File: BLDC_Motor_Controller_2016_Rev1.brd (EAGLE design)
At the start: 112.4 x 80 mm, 103 parts, among them J1 SERVOMOLEX_SL_THRU_HOLE, J3 APP_2POS_CONFIG5V_HORIZ, Q1 MOSFET-NCHANNELFQP30N06L, Q2 MOSFET-NCHANNELFQP30N06L, Q3 MOSFET-NCHANNELFQP30N06L, Q4 MOSFET-NCHANNELFQP30N06L, Q5 MOSFET-NCHANNELFQP30N06L, Q6 MOSFET-NCHANNELFQP30N06L, Q7 MOSFET-PCHANNEL, Q8 MOSFET-PCHANNEL

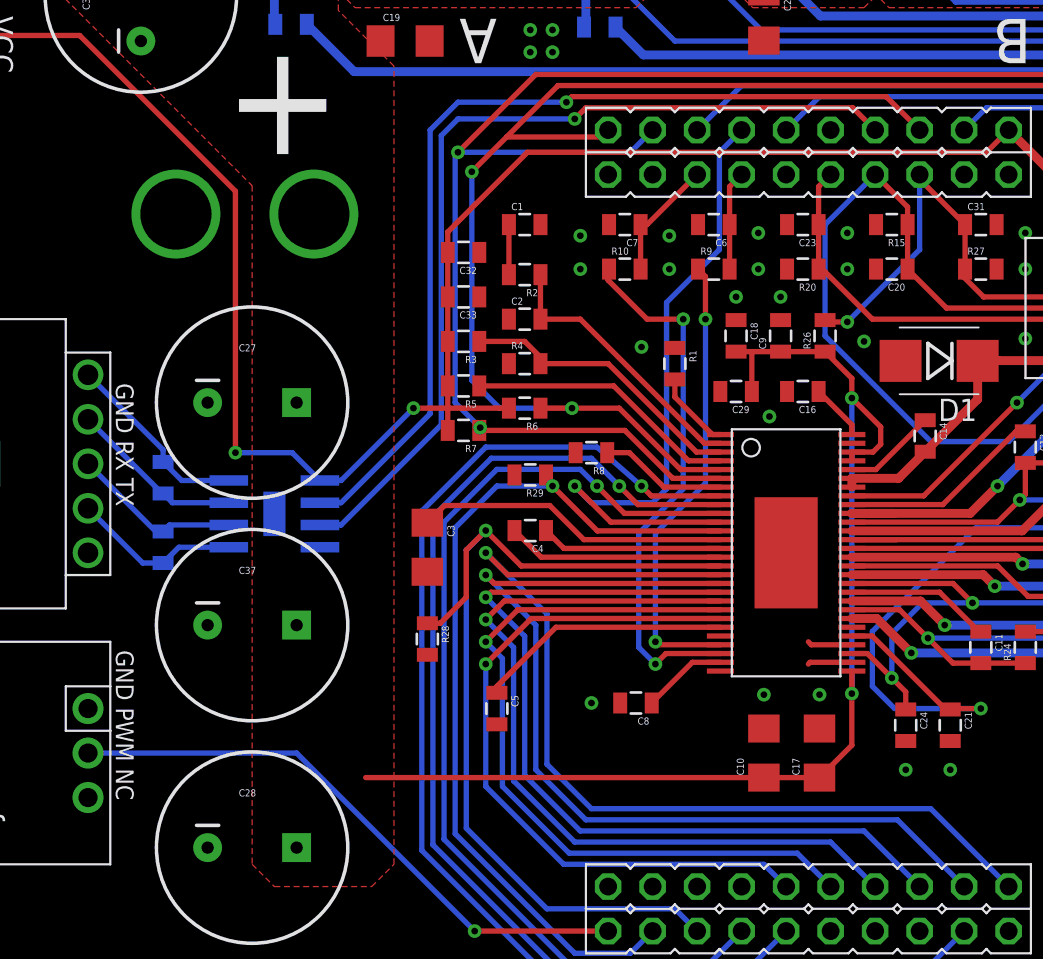
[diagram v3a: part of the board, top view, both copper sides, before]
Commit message: Minor routing changes
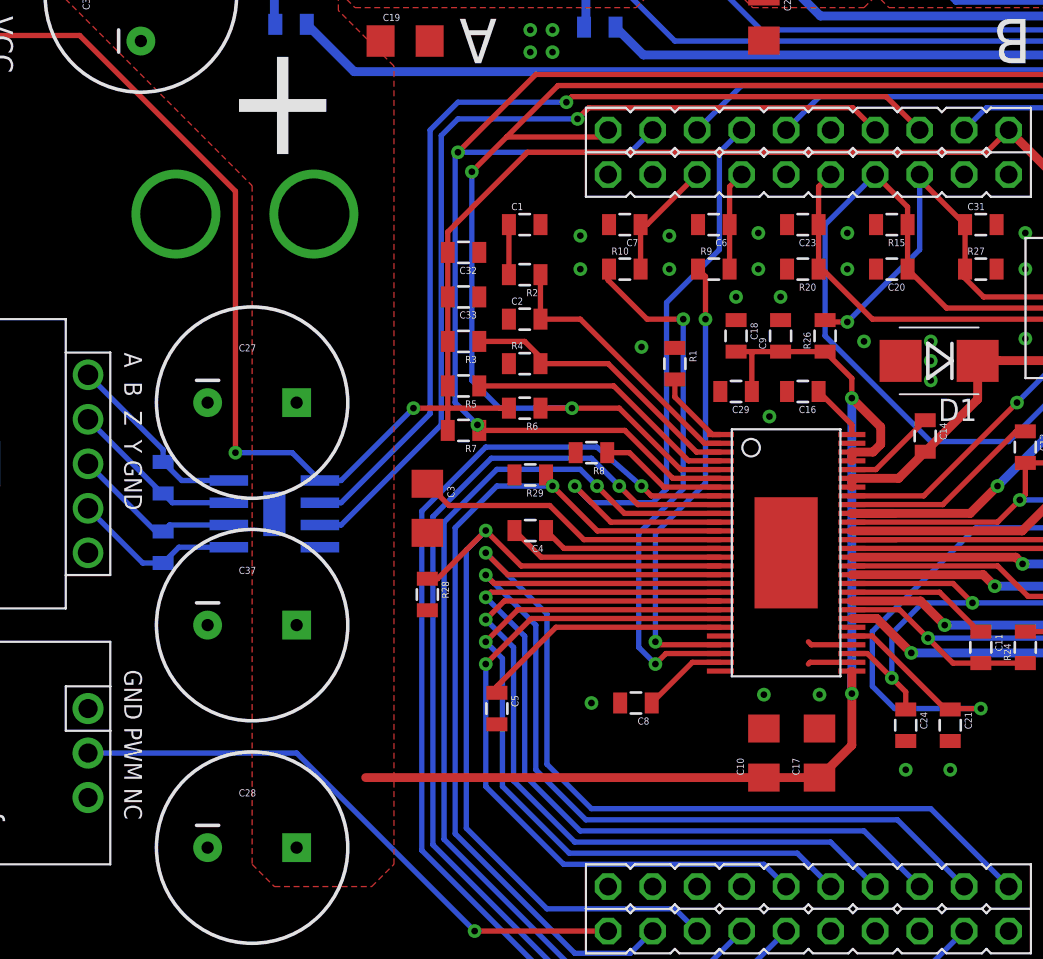
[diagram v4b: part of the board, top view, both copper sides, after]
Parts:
- moved R28 2.54 mm to (30.3, 23.0)
- moved C3 2.22 mm to (30.3, 27.9)
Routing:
- net EN_GATE: track 54.4 -> 51.8 mm
- net GND: vias 32 -> 35
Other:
- board text added: "A B Z Y GND"
- board text removed: "GND RX TX"
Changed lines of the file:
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@@
 <text x="5.3975" y="56.03875" size="1.27" layer="21" font="vector" rot="SR270">VCC</text>
 <text x="95.09125" y="19.3675" size="0.8128" layer="21" font="vector" rot="R90">Vcc C   B   A GND</text>
-<text x="12.54125" y="19.84375" size="1.016" layer="21" font="vector" rot="SR270">GND PWM NC</text>
+<text x="13.0175" y="18.7325" size="1.016" layer="21" font="vector" rot="SR270">GND PWM NC</text>
 <text x="101.9175" y="47.625" size="1.27" layer="21" font="vector" rot="SR90">FAULT</text>
 <text x="101.9175" y="41.5925" size="1.27" layer="21" font="vector" rot="SR90">OCTW</text>
@@
 <dimension x1="110.16" y1="-1.27" x2="110.16" y2="78.73" x3="127" y3="38.73" textsize="1.778" layer="47" unit="inch"/>
 <dimension x1="-3.4925" y1="-1.27" x2="110.16" y2="-1.27" x3="53.33375" y3="-21.59" textsize="1.778" layer="47" unit="inch"/>
-<text x="12.54125" y="35.08375" size="1.016" layer="21" font="vector" rot="SR270">GND RX TX</text>
 <text x="77.47" y="5.08" size="1.27" layer="21" font="vector" align="bottom-center">Missouri S&amp;T
 Mars Rover Design Team
@@
 Cameron Nichols
 </text>
+<text x="13.0175" y="36.83" size="1.016" layer="21" font="vector" rot="SR270">A  B  Z  Y GND</text>
 </plain>
 <attributes>
@@
 <element name="C26" library="SparkFun-Passives" package="0805" value="0.1u" x="66.9925" y="20.0025" rot="R270"/>
 <element name="C29" library="SparkFun-Passives" package="0805" value="0.1u" x="47.9425" y="34.6075" rot="R180"/>
-<element name="C3" library="SparkFun-Passives" package="1206" value="2.2u" x="30.32125" y="25.7175" rot="R270"/>
+<element name="C3" library="SparkFun-Passives" package="1206" value="2.2u" x="30.32125" y="27.94" rot="R270"/>
 <element name="C30" library="SparkFun-Passives" package="0805" value="0.01u" x="2.06375" y="65.88125" rot="R180"/>
 <element name="C31" library="SparkFun-Passives" package="0805" value="0.1u" x="61.9125" y="44.1325"/>
@@
 <element name="R26" library="SparkFun-Passives" package="0805" value="34.8k" x="53.0225" y="37.7825" rot="R90"/>
 <element name="R27" library="SparkFun-Passives" package="0805" value="4.99k" x="61.9125" y="41.5925"/>
-<element name="R28" library="SparkFun-Passives" package="0805" value="1k" x="30.32125" y="20.47875" rot="R270"/>
+<element name="R28" library="SparkFun-Passives" package="0805" value="1k" x="30.32125" y="23.01875" rot="R270"/>
 <element name="R29" library="SparkFun-Passives" package="0805" value="1k" x="36.195" y="29.845" rot="R180"/>
 <element name="R3" library="SparkFun-Passives" package="0805" value="31.6k" x="32.385" y="37.465" rot="R180"/>
@@
 <via x="44.1325" y="41.5925" extent="1-16" drill="0.381" shape="square"/>
 <via x="49.8475" y="33.17875" extent="1-16" drill="0.381" shape="square"/>
+<via x="59.055" y="37.465" extent="1-16" drill="0.381" shape="square"/>
+<via x="59.055" y="36.35375" extent="1-16" drill="0.381" shape="square"/>
+<via x="59.055" y="35.2425" extent="1-16" drill="0.381" shape="square"/>
 </signal>
 <signal name="N$3">
@@
 <wire x1="41.91" y1="48.26" x2="43.18" y2="49.53" width="0.3048" layer="16"/>
 <wire x1="33.285" y1="32.385" x2="33.285" y2="32.49125" width="0.3048" layer="1"/>
-<wire x1="33.285" y1="32.49125" x2="33.3375" y2="32.54375" width="0.3048" layer="1"/>
-<via x="33.3375" y="32.54375" extent="1-16" drill="0.381"/>
-<wire x1="33.3375" y1="32.54375" x2="31.90875" y2="33.9725" width="0.3048" layer="16"/>
+<wire x1="33.285" y1="32.49125" x2="33.17875" y2="32.7025" width="0.3048" layer="1"/>
+<via x="33.17875" y="32.7025" extent="1-16" drill="0.381"/>
+<wire x1="33.17875" y1="32.7025" x2="31.90875" y2="33.9725" width="0.3048" layer="16"/>
 <wire x1="31.90875" y1="33.9725" x2="31.90875" y2="48.10125" width="0.3048" layer="16"/>
 <wire x1="31.90875" y1="48.10125" x2="32.0675" y2="48.26" width="0.3048" layer="16"/>
@@
 <wire x1="47.05" y1="26.15" x2="39.255" y2="26.15" width="0.3048" layer="1"/>
 <wire x1="39.255" y1="26.15" x2="37.30625" y2="28.09875" width="0.3048" layer="1"/>
-<wire x1="37.30625" y1="28.09875" x2="31.3025" y2="28.09875" width="0.3048" layer="1"/>
-<wire x1="31.3025" y1="28.09875" x2="30.32125" y2="27.1175" width="0.3048" layer="1"/>
+<wire x1="37.30625" y1="28.09875" x2="31.5625" y2="28.09875" width="0.3048" layer="1"/>
+<wire x1="31.5625" y1="28.09875" x2="30.32125" y2="29.34" width="0.3048" layer="1"/>
 </signal>
 <signal name="EN_GATE">
@@
 <wire x1="44.45" y1="5.08" x2="37.1475" y2="5.08" width="0.3048" layer="16"/>
 <wire x1="37.1475" y1="5.08" x2="32.54375" y2="9.68375" width="0.3048" layer="16"/>
-<wire x1="30.32125" y1="21.37875" x2="31.0625" y2="21.37875" width="0.3048" layer="1"/>
-<wire x1="31.0625" y1="21.37875" x2="32.54375" y2="22.86" width="0.3048" layer="1"/>
-<wire x1="32.54375" y1="22.86" x2="32.54375" y2="25.55875" width="0.3048" layer="1"/>
-<wire x1="32.54375" y1="25.55875" x2="33.655" y2="26.67" width="0.3048" layer="1"/>
+<wire x1="30.32125" y1="23.91875" x2="30.90375" y2="23.91875" width="0.3048" layer="1"/>
+<wire x1="30.90375" y1="23.91875" x2="33.655" y2="26.67" width="0.3048" layer="1"/>
 </signal>
 <signal name="INH_A">
@@
 <contactref element="C37" pad="1"/>
 <contactref element="D6" pad="A"/>
-<wire x1="54.55" y1="31.15" x2="54.55" y2="30.65" width="0.3048" layer="1"/>
+<wire x1="54.55" y1="31.15" x2="54.55" y2="30.65" width="0.508" layer="1"/>
 <contactref element="C27" pad="1"/>
 <contactref element="C28" pad="1"/>
 <wire x1="52.73375" y1="12.54125" x2="52.705" y2="12.57" width="0.3048" layer="1"/>
-<wire x1="54.55" y1="17.36375" x2="54.55" y2="14.415" width="0.3048" layer="1"/>
-<wire x1="54.55" y1="14.415" x2="52.705" y2="12.57" width="0.3048" layer="1"/>
-<wire x1="54.55" y1="18.65" x2="54.55" y2="17.36375" width="0.3048" layer="1"/>
+<wire x1="54.55" y1="17.36375" x2="54.55" y2="14.415" width="0.508" layer="1"/>
+<wire x1="54.55" y1="14.415" x2="52.705" y2="12.57" width="0.508" layer="1"/>
+<wire x1="54.55" y1="18.65" x2="54.55" y2="17.36375" width="0.508" layer="1"/>
 <via x="54.55" y="17.36375" extent="1-16" drill="0.381"/>
-<wire x1="54.55" y1="17.36375" x2="54.55" y2="34.23" width="0.3048" layer="16"/>
+<wire x1="54.55" y1="17.36375" x2="54.55" y2="34.23" width="0.508" layer="16"/>
 <via x="54.55" y="34.23" extent="1-16" drill="0.381"/>
 <polygon width="0.3048" layer="1" thermals="no">
@@
 <contactref element="C35" pad="1"/>
 <contactref element="C34" pad="1"/>
-<wire x1="49.53" y1="12.57" x2="26.8" y2="12.57" width="0.3048" layer="1"/>
-<wire x1="49.53" y1="12.57" x2="52.705" y2="12.57" width="0.3048" layer="1"/>
+<wire x1="49.53" y1="12.57" x2="26.8" y2="12.57" width="0.508" layer="1"/>
+<wire x1="49.53" y1="12.57" x2="52.705" y2="12.57" width="0.508" layer="1"/>
 <wire x1="54.55" y1="34.23" x2="54.55" y2="35.355" width="0.3048" layer="1"/>
 <wire x1="54.55" y1="35.355" x2="53.0225" y2="36.8825" width="0.3048" layer="1"/>
@@
 <wire x1="48.895" y1="36.8825" x2="47.9425" y2="36.8825" width="0.3048" layer="1"/>
 <wire x1="48.8425" y1="34.6075" x2="48.8425" y2="36.83" width="0.3048" layer="1"/>
-<wire x1="56.1975" y1="32.5825" x2="54.55" y2="34.23" width="0.3048" layer="1"/>
-<wire x1="54.55" y1="31.15" x2="55.75625" y2="31.15" width="0.3048" layer="1"/>
-<wire x1="55.75625" y1="31.15" x2="56.1975" y2="31.59125" width="0.3048" layer="1"/>
-<wire x1="56.1975" y1="31.59125" x2="56.1975" y2="32.5825" width="0.3048" layer="1"/>
+<wire x1="56.1975" y1="32.5825" x2="54.55" y2="34.23" width="0.508" layer="1"/>
+<wire x1="54.55" y1="31.15" x2="55.75625" y2="31.15" width="0.508" layer="1"/>
+<wire x1="55.75625" y1="31.15" x2="56.1975" y2="31.59125" width="0.508" layer="1"/>
+<wire x1="56.1975" y1="31.59125" x2="56.1975" y2="32.5825" width="0.508" layer="1"/>
 <contactref element="J3" pad="5V"/>
 <wire x1="3.56375" y1="58.7375" x2="9.8425" y2="58.7375" width="0.3048" layer="1"/>
@@
 <signal name="TX">
 <contactref element="U$2" pad="PB1"/>
-<via x="38.735" y="50.165" extent="1-16" drill="0.381"/>
-<wire x1="38.735" y1="50.165" x2="39.37" y2="50.8" width="0.3048" layer="1"/>
-<wire x1="39.37" y1="50.8" x2="54.61" y2="50.8" width="0.3048" layer="1"/>
+<via x="38.89375" y="50.165" extent="1-16" drill="0.381"/>
+<wire x1="38.89375" y1="50.165" x2="39.52875" y2="50.8" width="0.3048" layer="1"/>
+<wire x1="39.52875" y1="50.8" x2="54.61" y2="50.8" width="0.3048" layer="1"/>
 <wire x1="54.61" y1="50.8" x2="55.88" y2="49.53" width="0.3048" layer="1"/>
 <wire x1="31.115" y1="32.7025" x2="31.115" y2="49.2125" width="0.3048" layer="16"/>
 <wire x1="31.115" y1="49.2125" x2="32.0675" y2="50.165" width="0.3048" layer="16"/>
-<wire x1="32.0675" y1="50.165" x2="38.735" y2="50.165" width="0.3048" layer="16"/>
+<wire x1="32.0675" y1="50.165" x2="38.89375" y2="50.165" width="0.3048" layer="16"/>
 <contactref element="U$3" pad="3"/>
 <wire x1="31.115" y1="32.7025" x2="25.4" y2="26.9875" width="0.3048" layer="16"/>

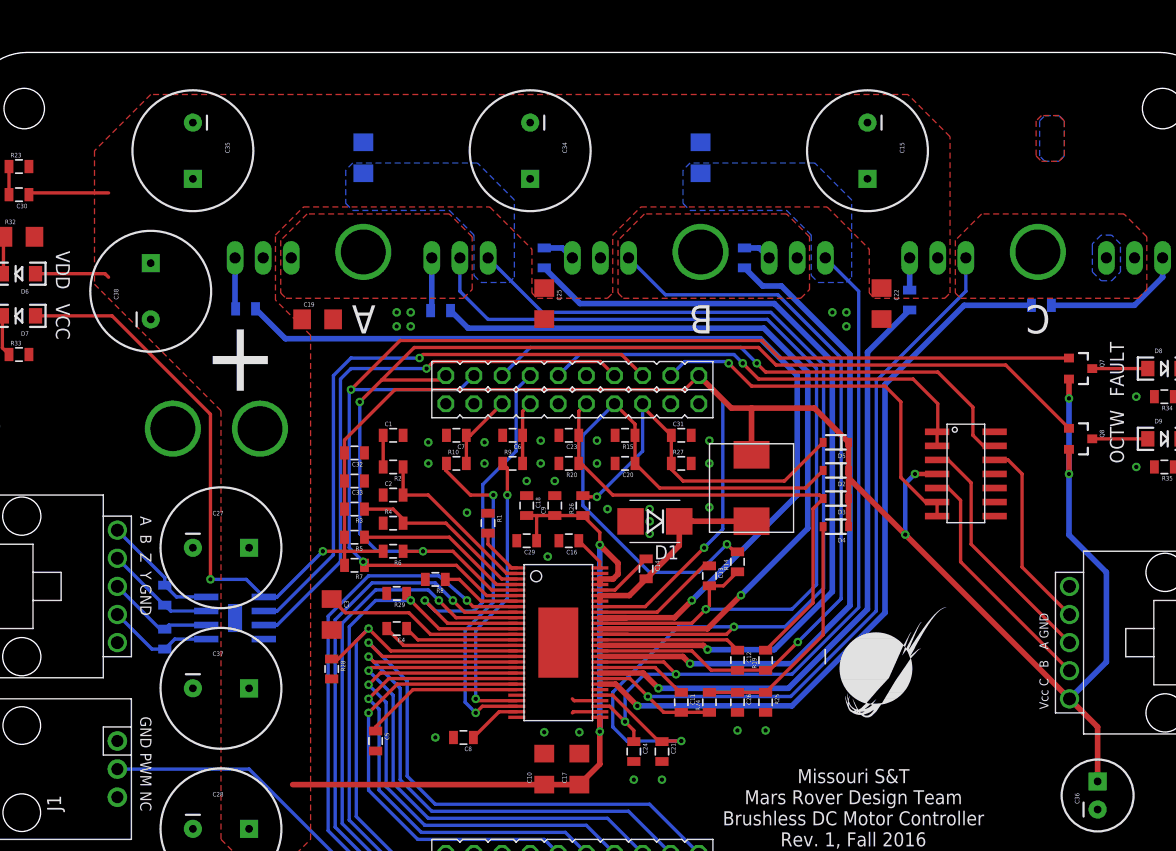
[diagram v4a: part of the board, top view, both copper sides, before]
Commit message: Improved routing
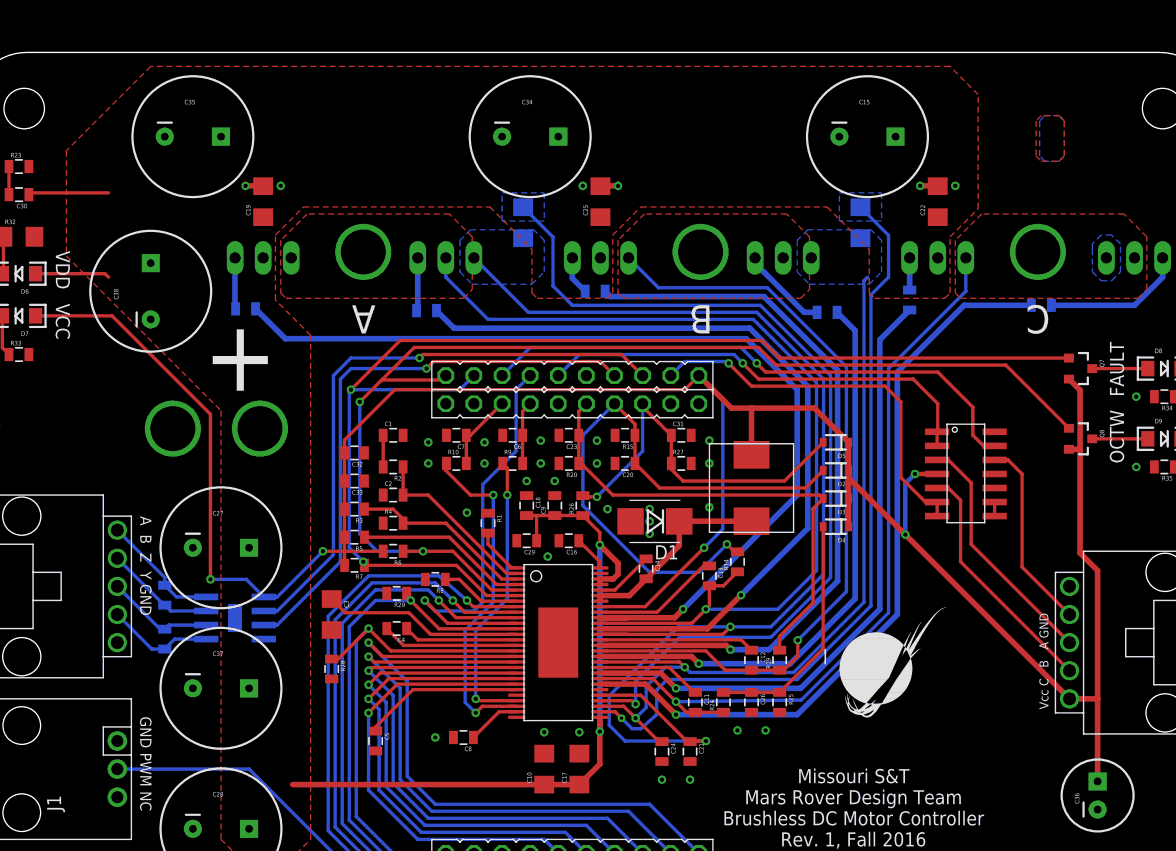
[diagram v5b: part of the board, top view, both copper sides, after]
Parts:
- moved R18 15.6 mm to (78.1, 63.3)
- moved R13 15.6 mm to (47.6, 63.3)
- moved C19 11.7 mm to (24.1, 65.2), turned to 90 degrees
- moved C22 10.5 mm to (85.1, 65.2), turned to 90 degrees
- moved C25 10.5 mm to (54.6, 65.2), turned to 90 degrees
- moved R17 8.94 mm to (75.1, 55.2), turned to 180 degrees
- moved R16 5.50 mm to (54.1, 57.1), turned to 180 degrees
- moved C21 2.54 mm to (62.7, 15.6)
- moved C24 2.54 mm to (60.2, 15.6)
- moved C15 1.27 mm to (78.7, 71.1), turned to 0 degrees
- moved C34 1.27 mm to (48.3, 71.1), turned to 0 degrees
- moved C35 1.27 mm to (17.8, 71.1), turned to 0 degrees
- moved R12 1.27 mm to (38.9, 55.4)
- moved C11 1.27 mm to (63.2, 20.0)
- moved C12 1.27 mm to (68.3, 23.8)
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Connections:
- new net N$40: U$13.8, U$13.9
- new net SP1: C21.2, R13.1, U$1.32
- new net SP2: C24.2, R18.1, U$1.30
- net GND: no longer C21.2, C24.2, R13.1, R18.1, U$1.30, U$1.32
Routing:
- net SP1: track 0.00 -> 81.9 mm, vias 0 -> 1
- net SP2: track 0.00 -> 68.7 mm, vias 0 -> 1
- net GL_B: track 60.5 -> 52.3 mm
- net GH_B: track 73.7 -> 67.2 mm
- net N$15: track 2.60 -> 7.93 mm
- net SL_A: track 111.4 -> 115.7 mm
- net VCC: track 234.0 -> 232.6 mm, vias 7 -> 5
- net GL_C: track 66.9 -> 68.3 mm
- net N$40: track 0.00 -> 1.27 mm
- net N$25: track 12.8 -> 14.1 mm
- net N$21: track 8.59 -> 9.86 mm
- net SL_B: track 72.0 -> 70.8 mm
- net SH_A: track 84.0 -> 83.0 mm
- net SH_B: track 69.9 -> 70.9 mm
- net GH_A: track 87.1 -> 86.3 mm
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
